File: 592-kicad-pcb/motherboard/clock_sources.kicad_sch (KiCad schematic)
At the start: 18 parts, among them J1 U.FL, U1 SN74LVC1G3157DBVR, U2 SMXS-04K, U3 SN74LVC1G3157DBVR, U8 74LVC1T45GW, Y1 Si5351A, Y2 NX3225GA-25.000M-STD-CRG-2

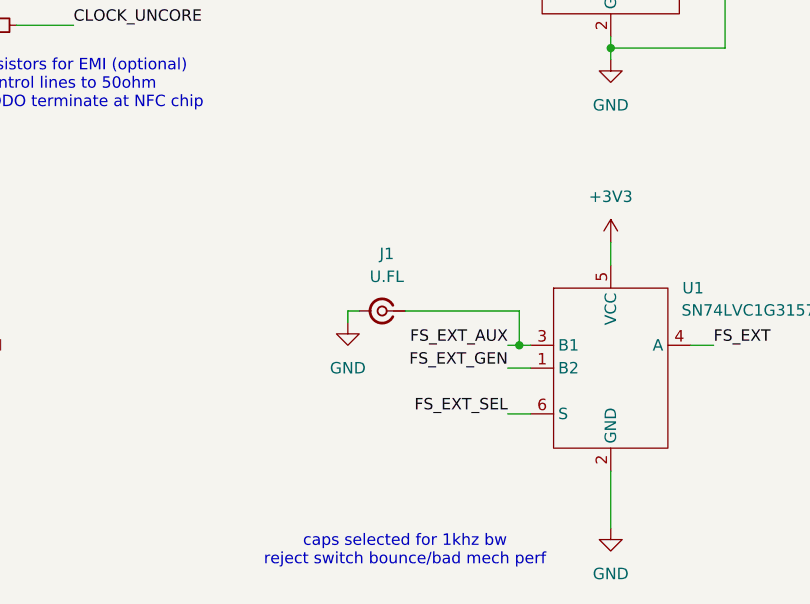
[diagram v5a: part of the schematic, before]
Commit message: clean up some pull up/downs
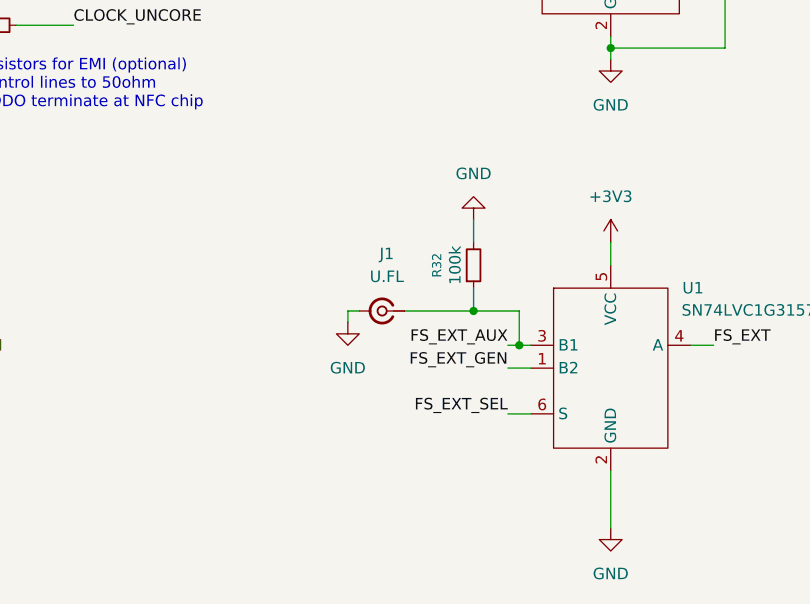
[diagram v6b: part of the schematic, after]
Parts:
- added R32: 100k, Capacitor_SMD:C_0603_1608Metric, symbol Device:R_Small
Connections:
- net FS_EXT_AUX: now also R32.1
- net GND: now also R32.2
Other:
- note removed: "caps selected for 1khz bw reject switch bounce/bad mech perf"
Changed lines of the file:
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@@
-		)
-	)
-	(text "caps selected for 1khz bw\nreject switch bounce/bad mech perf"
-		(exclude_from_sim no)
-		(at 137.16 140.97 0)
-		(effects
-			(font
-				(size 1.27 1.27)
-			)
 		)
 	)
@@
 	)
 	(junction
+		(at 144.78 114.3)
+		(diameter 0)
+		(color 0 0 0 0)
+	)
+	(junction
 		(at 148.59 35.56)
 		(diameter 0)
@@
 	(wire
 		(pts
-			(xy 137.16 114.3) (xy 149.86 114.3)
+			(xy 137.16 114.3) (xy 144.78 114.3)
 		)
 		(stroke
@@
 	(wire
 		(pts
+			(xy 144.78 104.14) (xy 144.78 106.68)
+		)
+		(stroke
+			(width 0)
+			(type default)
+		)
+	)
+	(wire
+		(pts
 			(xy 148.59 125.73) (xy 151.13 125.73)
 		)
@@
 	(wire
 		(pts
+			(xy 144.78 114.3) (xy 149.86 114.3)
+		)
+		(stroke
+			(width 0)
+			(type default)
+		)
+	)
+	(wire
+		(pts
 			(xy 132.08 114.3) (xy 130.81 114.3)
+		)
+		(stroke
+			(width 0)
+			(type default)
+		)
+	)
+	(wire
+		(pts
+			(xy 144.78 111.76) (xy 144.78 114.3)
 		)
 		(stroke
@@
 				(path "/5b0c97ac-fa03-4db8-b41b-0eee32b6f55d/22c0ff7f-6fb8-476b-be54-e80d47691e23"
 					(reference "C5")
+					(unit 1)
+				)
+			)
+		)
+	)
+	(symbol
+		(lib_id "power:GND")
+		(at 144.78 104.14 180)
+		(unit 1)
+		(exclude_from_sim no)
+		(in_bom yes)
+		(on_board yes)
+		(dnp no)
+		(fields_autoplaced yes)
+		(property "Reference" "#PWR085"
+			(at 144.78 97.79 0)
+			(effects
+				(font
+					(size 1.27 1.27)
+				)
+				(hide yes)
+			)
+		)
+		(property "Value" "GND"
+			(at 144.78 99.06 0)
+			(effects
+				(font
+					(size 1.27 1.27)
+				)
+			)
+		)
+		(property "Footprint" ""
+			(at 144.78 104.14 0)
+			(effects
+				(font
+					(size 1.27 1.27)
+				)
+				(hide yes)
+			)
+		)
+		(property "Datasheet" ""
+			(at 144.78 104.14 0)
+			(effects
+				(font
+					(size 1.27 1.27)
+				)
+				(hide yes)
+			)
+		)
+		(property "Description" "Power symbol creates a global label with name \"GND\" , ground"
+			(at 144.78 104.14 0)
+			(effects
+				(font
+					(size 1.27 1.27)
+				)
+				(hide yes)
+			)
+		)
+		(pin "1"
+		)
+		(instances
+			(project "motherboard"
+				(path "/5b0c97ac-fa03-4db8-b41b-0eee32b6f55d/22c0ff7f-6fb8-476b-be54-e80d47691e23"
+					(reference "#PWR085")
 					(unit 1)
 				)
@@
 					(unit 1)
 				)
+			)
+		)
+	)
+	(symbol
+		(lib_id "Device:R_Small")
+		(at 144.78 109.22 0)
+		(mirror x)
+		(unit 1)
+		(exclude_from_sim no)
+		(in_bom yes)
+		(on_board yes)
+		(dnp no)
+		(property "Reference" "R32"
+			(at 140.716 109.22 90)
+			(effects
+				(font
+					(size 1.016 1.016)
+				)
+			)
+		)
+		(property "Value" "100k"
+			(at 142.748 109.22 90)
+			(effects
+				(font
+					(size 1.27 1.27)
+				)
+			)
+		)
+		(property "Footprint" "Capacitor_SMD:C_0603_1608Metric"
+			(at 144.78 109.22 0)
+			(effects
+				(font
+					(size 1.27 1.27)
+				)
+				(hide yes)
+			)
+		)
+		(property "Datasheet" "~"
+			(at 144.78 109.22 0)
+			(effects
+				(font
+					(size 1.27 1.27)
+				)
+				(hide yes)
+			)
+		)
+		(property "Description" "Resistor, small symbol"
+			(at 144.78 109.22 0)
+			(effects
+				(font
+					(size 1.27 1.27)
+				)
+				(hide yes)
+			)
+		)
+		(pin "2"
+		)
+		(pin "1"
+		)
+		(instances
+			(project "motherboard"
+				(path "/5b0c97ac-fa03-4db8-b41b-0eee32b6f55d/22c0ff7f-6fb8-476b-be54-e80d47691e23"
+					(reference "R32")
+					(unit 1)
+				)

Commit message: add jlc stackup, size pulldowns
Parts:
- R14, R15, R3, R32, R4, R5: footprint Capacitor_SMD:C_0603_1608Metric -> Resistor_SMD:R_0603_1608Metric
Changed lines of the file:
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@@
 			)
 		)
-		(property "Footprint" "Capacitor_SMD:C_0603_1608Metric"
+		(property "Footprint" "Resistor_SMD:R_0603_1608Metric"
 			(at 91.44 82.55 0)
 			(effects
@@
 			)
 		)
-		(property "Footprint" "Capacitor_SMD:C_0603_1608Metric"
+		(property "Footprint" "Resistor_SMD:R_0603_1608Metric"
 			(at 91.44 72.39 0)
 			(effects
@@
 			)
 		)
-		(property "Footprint" "Capacitor_SMD:C_0603_1608Metric"
+		(property "Footprint" "Resistor_SMD:R_0603_1608Metric"
 			(at 144.78 109.22 0)
 			(effects
@@
 			)
 		)
-		(property "Footprint" "Capacitor_SMD:C_0603_1608Metric"
+		(property "Footprint" "Resistor_SMD:R_0603_1608Metric"
 			(at 91.44 77.47 0)
 			(effects
@@
 			)
 		)
-		(property "Footprint" "Capacitor_SMD:C_0603_1608Metric"
+		(property "Footprint" "Resistor_SMD:R_0603_1608Metric"
 			(at 199.39 29.21 0)
 			(effects
@@
 			)
 		)
-		(property "Footprint" "Capacitor_SMD:C_0603_1608Metric"
+		(property "Footprint" "Resistor_SMD:R_0603_1608Metric"
 			(at 191.77 29.21 0)
 			(effects

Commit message: rough layout stufF
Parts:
- added JP1, JP2: Jumper_2_Small_Bridged, Jumper:SolderJumper-2_P1.3mm_Bridged_RoundedPad1.0x1.5mm, symbol Jumper:Jumper_2_Small_Bridged
- R3, R4, R5: value 0 -> 10
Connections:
- net EXT_CLK_DIG_SEL: now also C10.2, R14.1, U2.8 (1o); no longer C11.2, R15.1, U2.7 (2o)
- net FS_EXT_SEL: now also C11.2, R15.1, U2.6 (3o); no longer C10.2, R14.1, U2.8 (1o)
- net GND: now also U2.7 (2o), JP1.1 (A), JP2.2 (B); no longer U2.6 (3o)
- net at C5.1, Y2.2: now also JP1.2 (B)
- net at C6.1, Y2.4: now also JP2.1 (A)
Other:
- note removed: "resistors for EMI (optional) control lines to 50ohm TODO terminate at NFC chip"
